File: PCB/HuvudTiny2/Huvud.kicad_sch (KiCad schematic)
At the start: 106 parts, among them J1 MOLEX Micro Fit 2x3, J10 FAN0, J2 DBG, J3 THERM, J4 FAN1, J5 FAN2, J6 Heater, J7 Endstop, J8 THERM, J9 STEPPER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

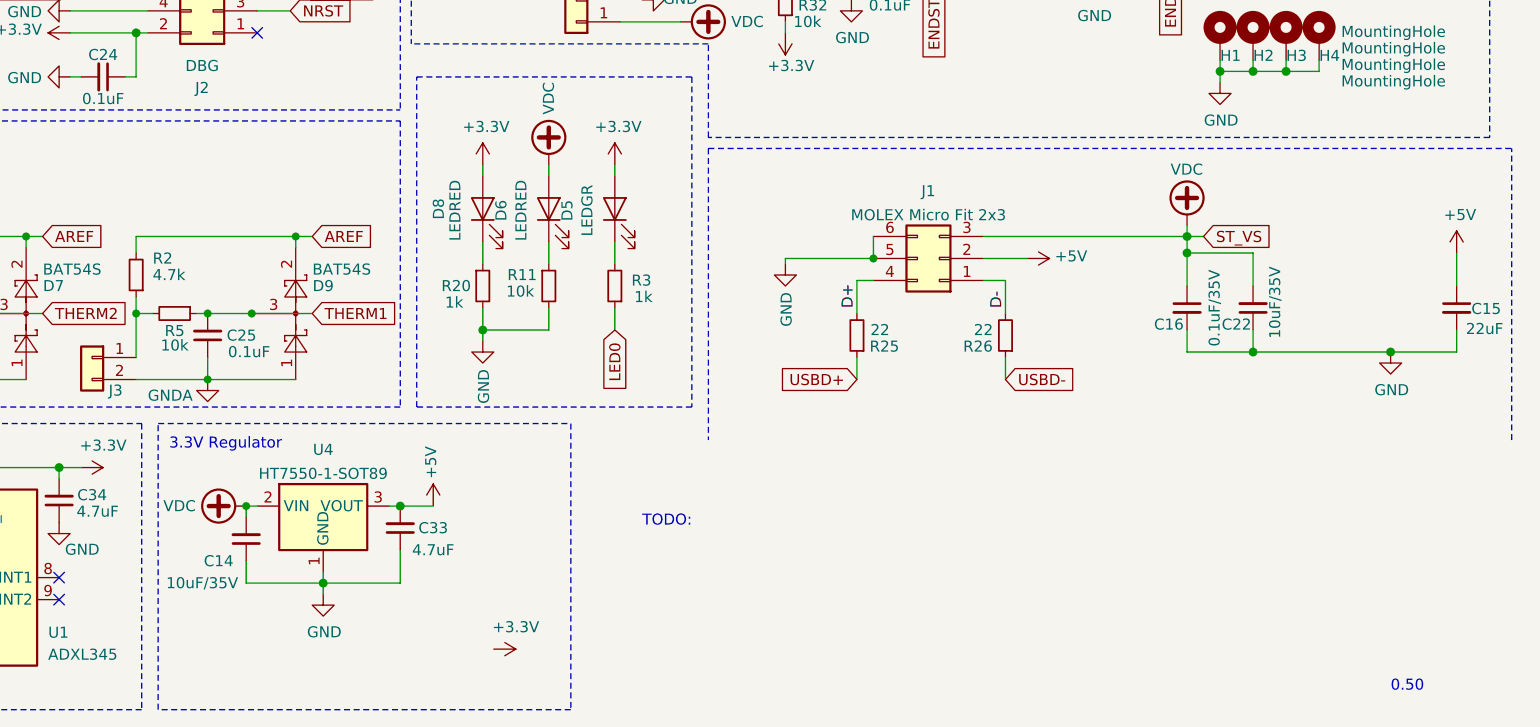
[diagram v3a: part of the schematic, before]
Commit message: Re work power supply added 5V stage: 24v->5V->3.3V
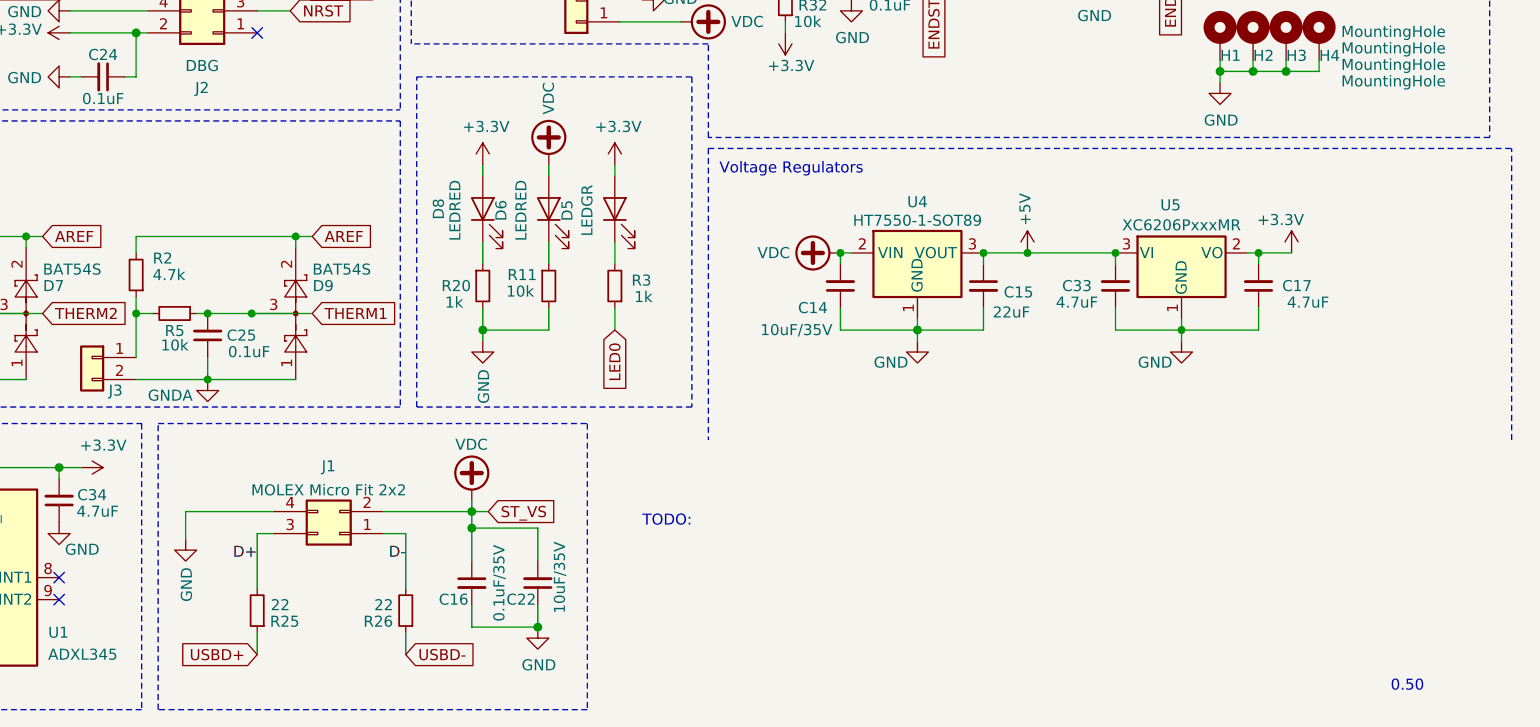
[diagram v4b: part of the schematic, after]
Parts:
- added C17: 4.7uF, Capacitor_SMD:C_0402_1005Metric, symbol Device:C_Small
- added U5: XC6206PxxxMR, Package_TO_SOT_SMD:SOT-23, symbol Regulator_Linear:XC6206PxxxMR
- J1: value MOLEX Micro Fit 2x3 -> MOLEX Micro Fit 2x2; footprint Connector_Molex:Molex_Micro-Fit_3.0_43045-0600_2x03_P3.00mm_Horizontal -> Connector_Molex:Molex_Micro-Fit_3.0_43045-0400_2x02_P3.00mm_Horizontal; symbol Connector_Generic:Conn_02x03_Top_Bottom -> Connector_Generic:Conn_02x02_Top_Bottom
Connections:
- net +3V3: now also C17.2, U5.2 (VO)
- net +5V: now also U5.3 (VI); no longer J1.2 (Pin_2)
- net D+: now also J1.3 (Pin_3); no longer J1.4 (Pin_4)
- net GND: now also J1.4 (Pin_4), C17.1, U5.1 (GND); no longer J1.5 (Pin_5), J1.6 (Pin_6)
- net VDC: now also J1.2 (Pin_2); no longer J1.3 (Pin_3)
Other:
- note added: "Voltage Regulators"
- note removed: "3.3V Regulator"
- moved on the sheet: C14, C15, C16, C22, C33, R25, R26, U4

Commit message: Add LCSC component for the MCU.
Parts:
- U3: LCSC (none) -> C220692
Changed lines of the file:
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@@
+      (effects (font (size 1.27 1.27)) hide)
+    )
+    (property "LCSC" "C220692" (id 4) (at 85.09 54.61 90)
       (effects (font (size 1.27 1.27)) hide)
     )

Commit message: Update fabrication files.
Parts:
- D4: LCSC C406049 -> C364278
- J1: LCSC (none) -> C122413
- J10, J3, J4, J5, J8: LCSC C506675 -> C10819
- J6: LCSC C557685 -> C122431
- J7: LCSC C530977 -> C10823
- Q3: LCSC C115844 -> C341712
- Y1: LCSC C32346 -> C271654
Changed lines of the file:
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@@
       (effects (font (size 1.27 1.27)) hide)
     )
-    (property "LCSC" "C32346" (id 4) (at 37.465 83.185 0)
+    (property "LCSC" "C271654" (id 4) (at 37.465 83.185 0)
       (effects (font (size 1.27 1.27)) hide)
     )
@@
       (effects (font (size 1.27 1.27)) hide)
     )
-    (property "LCSC" "C406049" (id 4) (at 194.945 109.22 0)
+    (property "LCSC" "C364278" (id 4) (at 194.945 109.22 0)
       (effects (font (size 1.27 1.27)) hide)
     )
@@
       (effects (font (size 1.27 1.27)) hide)
     )
-    (property "LCSC" "C506675" (id 4) (at 27.305 114.935 0)
+    (property "LCSC" "C10819" (id 4) (at 27.305 114.935 0)
       (effects (font (size 1.27 1.27)) hide)
     )
@@
       (effects (font (size 1.27 1.27)) hide)
     )
-    (property "LCSC" "C506675" (id 4) (at 27.305 147.32 0)
+    (property "LCSC" "C10819" (id 4) (at 27.305 147.32 0)
       (effects (font (size 1.27 1.27)) hide)
     )
@@
       (effects (font (size 1.27 1.27)) hide)
     )
-    (property "LCSC" "C557685" (id 4) (at 29.845 175.26 0)
+    (property "LCSC" "C122431" (id 4) (at 29.845 175.26 0)
       (effects (font (size 1.27 1.27)) hide)
     )
@@
       (effects (font (size 1.27 1.27)) hide)
     )
-    (property "LCSC" "C506675" (id 4) (at 52.705 125.095 0)
+    (property "LCSC" "C10819" (id 4) (at 52.705 125.095 0)
       (effects (font (size 1.27 1.27)) hide)
     )
@@
       (effects (font (size 1.27 1.27)) hide)
     )
-    (property "LCSC" "C506675" (id 4) (at 88.265 155.575 0)
+    (property "LCSC" "C10819" (id 4) (at 88.265 155.575 0)
       (effects (font (size 1.27 1.27)) hide)
     )
@@
       (effects (font (size 1.27 1.27)) hide)
     )
-    (property "LCSC" "C506675" (id 4) (at 119.38 155.575 0)
+    (property "LCSC" "C10819" (id 4) (at 119.38 155.575 0)
       (effects (font (size 1.27 1.27)) hide)
     )
@@
       (effects (font (size 1.27 1.27)) hide)
     )
+    (property "LCSC" "C122413" (id 4) (at 147.955 175.895 0)
+      (effects (font (size 1.27 1.27)) hide)
+    )
     (pin "1")
     (pin "2")
@@
       (effects (font (size 1.27 1.27)) (justify left) hide)
     )
-    (property "LCSC" "C115844" (id 4) (at 36.83 170.18 0)
+    (property "LCSC" " C341712" (id 4) (at 36.83 170.18 0)
       (effects (font (size 1.27 1.27)) hide)
     )
@@
       (effects (font (size 1.27 1.27)) hide)
     )
-    (property "LCSC" "C530977" (id 4) (at 175.26 111.76 0)
-      (effects (font (size 1.27 1.27)) hide)
-    )
+    (property "LCSC" "C10823" (id 4) (at 175.26 111.76 0)
+      (effects (font (size 1.27 1.27)) hide)
+    )

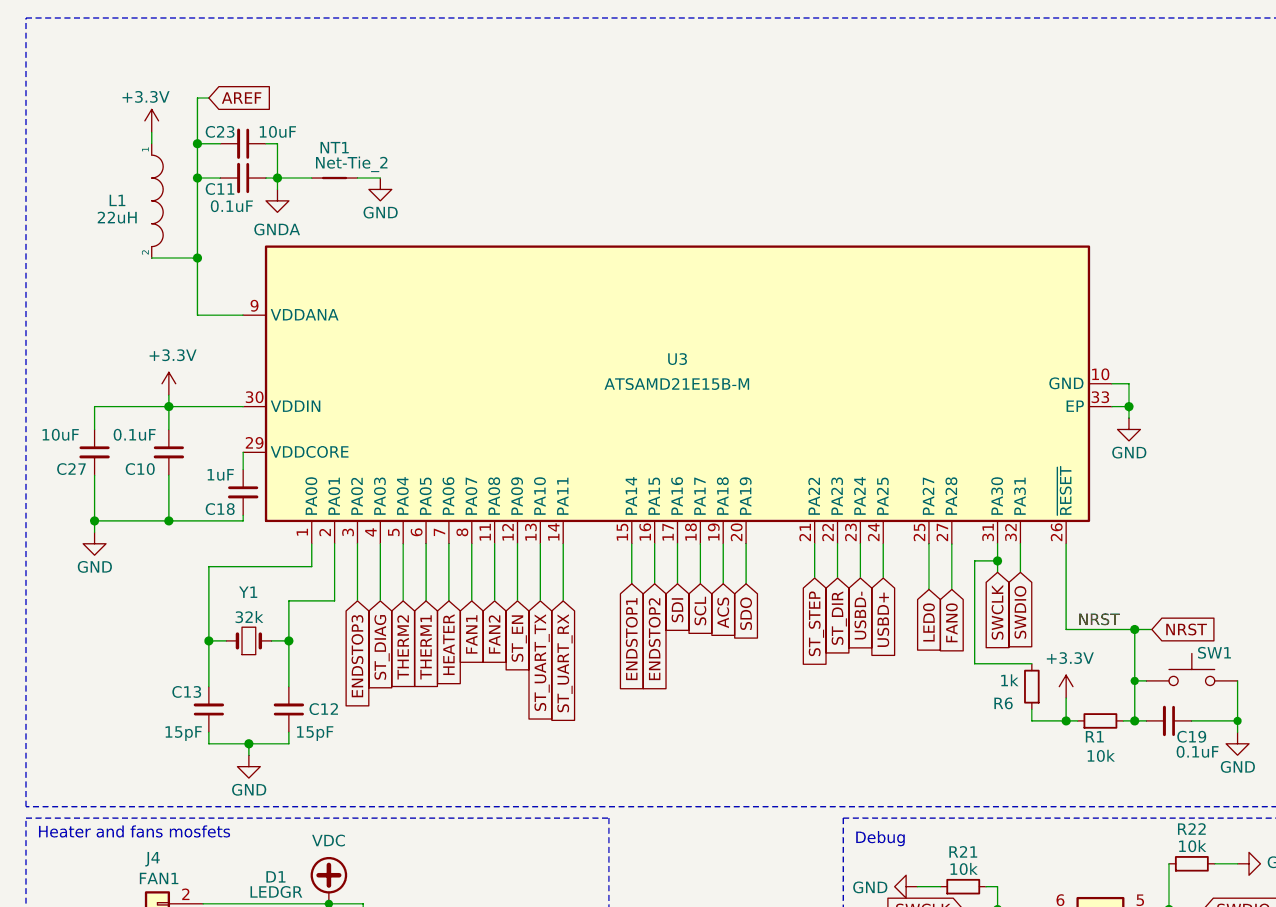
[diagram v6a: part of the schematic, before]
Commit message: Remove SAMD21 part update chrystal to 12MHz.
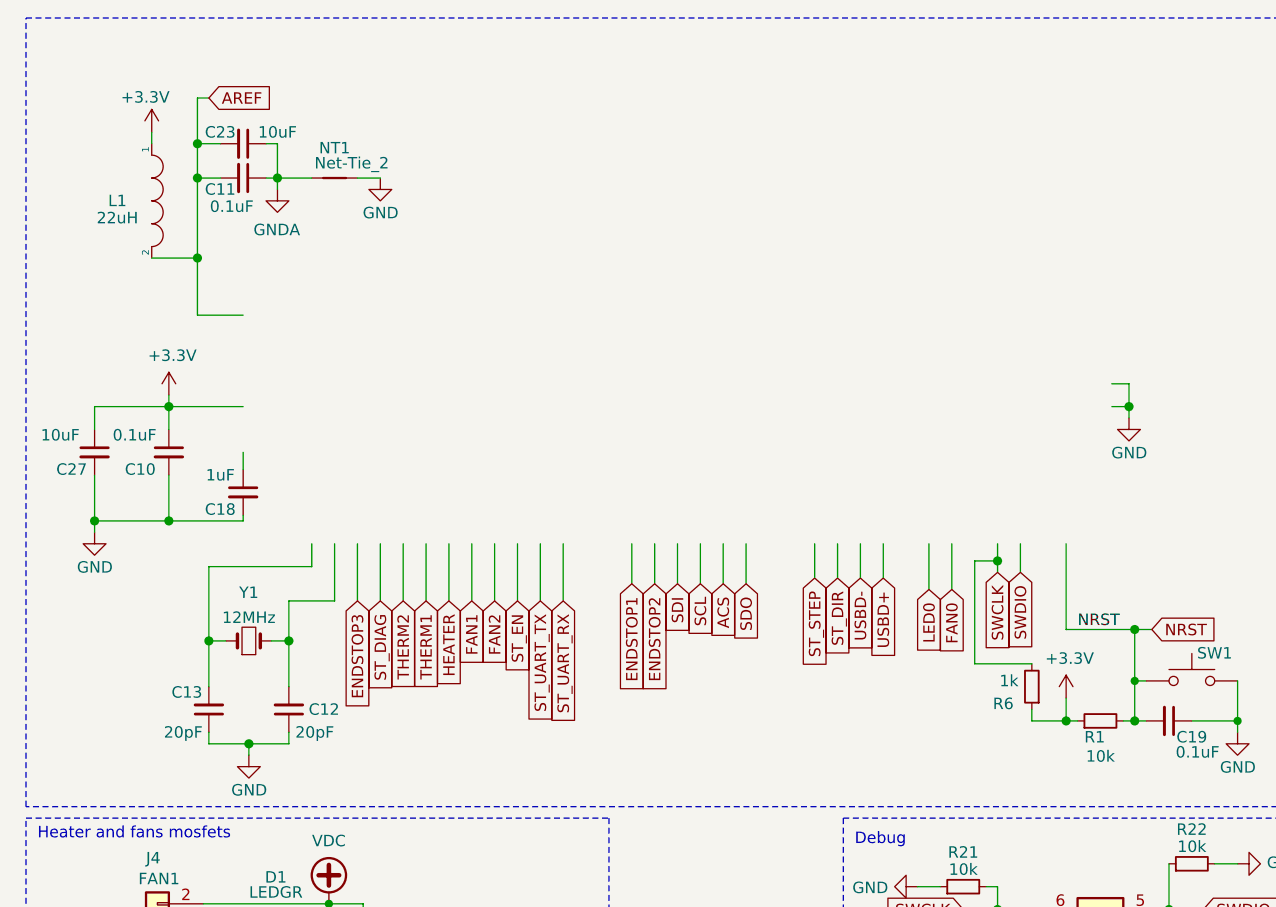
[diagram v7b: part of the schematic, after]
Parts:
- removed U3: ATSAMD21E15B-M, Package_DFN_QFN:QFN-32-1EP_5x5mm_P0.5mm_EP3.6x3.6mm, symbol MCU_Microchip_SAMD:ATSAMD21E15B-M
- C12, C13: value 15pF -> 20pF; LCSC C1548 -> C1554
- Y1: value 32k -> 12MHz; footprint Crystal:Crystal_SMD_3215-2Pin_3.2x1.5mm -> Crystal:Crystal_SMD_3225-4Pin_3.2x2.5mm; LCSC C271654 -> C9002
